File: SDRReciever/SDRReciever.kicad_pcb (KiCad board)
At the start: 2 copper layers, 100 x 100 mm, 78 parts, among them J1 Conn_Coaxial, J10 I_0, J11 I_180, J12 Q_90, J13 Q_270, J14 I_OUT, J15 Q_OUT, J16 5V, J17 4.3V, J18 Conn_01x02_Female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

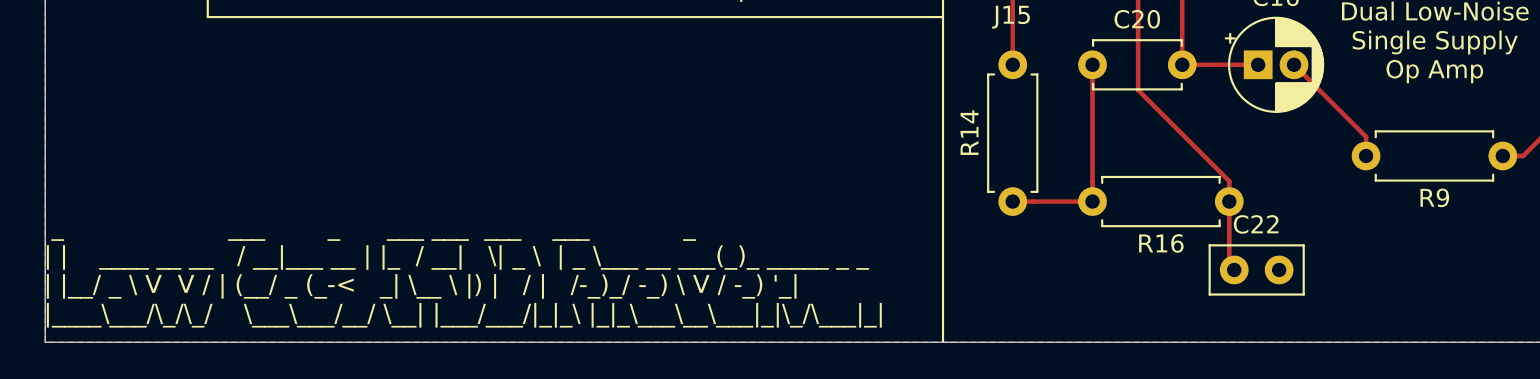
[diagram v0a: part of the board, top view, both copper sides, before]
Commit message: Changed PCB silkscreen title block, renamed some image files to be more specific to the revision they refer to, added SVGs for clearer documentation imagery
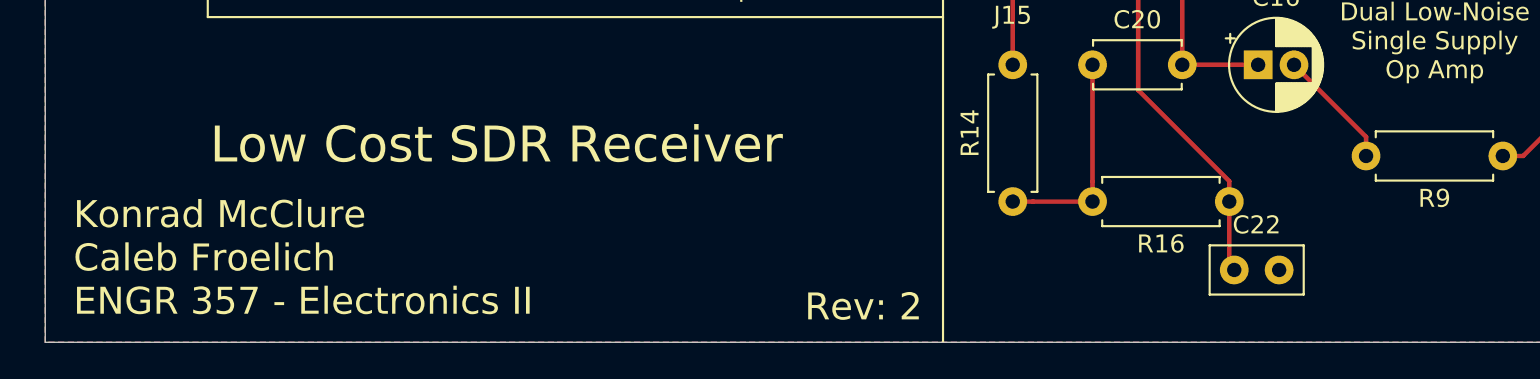
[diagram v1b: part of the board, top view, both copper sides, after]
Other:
- board text added: "Konrad McClure Caleb Froelich ENGR 357 - Electronics II"
- board text added: "Low Cost SDR Receiver"
- board text added: "Rev: 2"
- board text removed: "_ ___ _ ___ ___ ___ ___ _ | | ____ __ __ / __|___ __ | |_ / __| \| _ \ | _ \___ __ ___(_)_ _____ _ _ | |__/ _ \ V V / | (__/ _ (_-< _| \__ \ |) | / | /-_)_/ -_) \ V / -_) '_| |____\___/\_/\_/ \___\___/__/ \__| |___/___/|_|_\ |_|_\___\__\___|_|\_/\___|_|"
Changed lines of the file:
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@@
   (general
     (thickness 1.6)
-    (drawings 76)
+    (drawings 78)
     (tracks 386)
     (zones 0)
@@
     (44 Edge.Cuts user)
     (45 Margin user)
-    (46 B.CrtYd user)
-    (47 F.CrtYd user)
+    (46 B.CrtYd user hide)
+    (47 F.CrtYd user hide)
     (48 B.Fab user)
-    (49 F.Fab user)
+    (49 F.Fab user hide)
   )
   (setup
@@
     )
   )
-  (gr_text "  _                     ___        _      ___ ___  ___    ___            _             \n | |    ____ __ __   / __|___ __ | |_  / __|   \\| _ \\  | _ \\___ __ ___(_)_ _____ _ _ \n | |__/ _ \\ V  V / | (__/ _ (_-<   _| \\__ \\ |) |   / |   /-_)_/ -_) \\ V / -_) '_|\n |____\\___/\\_/\\_/    \\___\\___/__/ \\__| |___/___/|_|_\\ |_|_\\___\\__\\___|_|\\_/\\___|_| " (at 74.48 140.98) (layer F.SilkS)
-    (effects (font (size 1 1) (thickness 0.15)) (justify left))
+  (gr_text "Rev: 2" (at 120.59 143.03) (layer F.SilkS)
+    (effects (font (size 1.5 1.5) (thickness 0.2)))
+  )
+  (gr_text "Low Cost SDR Receiver" (at 100.14 134) (layer F.SilkS)
+    (effects (font (size 2 2) (thickness 0.3)))
+  )
+  (gr_text "Konrad McClure\nCaleb Froelich\nENGR 357 - Electronics II" (at 76.57 140.3) (layer F.SilkS)
+    (effects (font (size 1.5 1.5) (thickness 0.2)) (justify left))
   )
   (gr_line (start 103.474 112.252) (end 104.006 112.784) (layer F.SilkS) (width 0.12))
@@
       )
     )
+  )
+  (zone (net 0) (net_name "") (layers F&B.Cu) (hatch edge 0.508)
+    (connect_pads (clearance 0.508))
+    (min_thickness 0.254)
+    (keepout (tracks not_allowed) (vias not_allowed) (copperpour not_allowed))
+    (fill (arc_segments 32) (thermal_gap 0.508) (thermal_bridge_width 0.508))
+    (polygon
+      (pts
+        (xy 80.48 64.53) (xy 75.01 64.53) (xy 75.01 62.84) (xy 80.48 62.84)
+      )
+    )
+  )
+  (zone (net 0) (net_name "") (layers F&B.Cu) (hatch edge 0.508)
+    (connect_pads (clearance 0.508))
+    (min_thickness 0.254)
+    (keepout (tracks not_allowed) (vias not_allowed) (copperpour not_allowed))
+    (fill (arc_segments 32) (thermal_gap 0.508) (thermal_bridge_width 0.508))
+    (polygon
+      (pts
+        (xy 80.45 68.73) (xy 75.01 68.73) (xy 75.01 67.11) (xy 80.45 67.11)
+      )
+    )
